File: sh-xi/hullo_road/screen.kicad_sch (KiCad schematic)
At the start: 512 parts

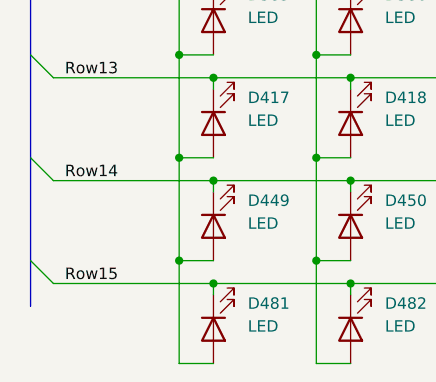
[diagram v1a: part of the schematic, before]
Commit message: Place LEDs in a grid
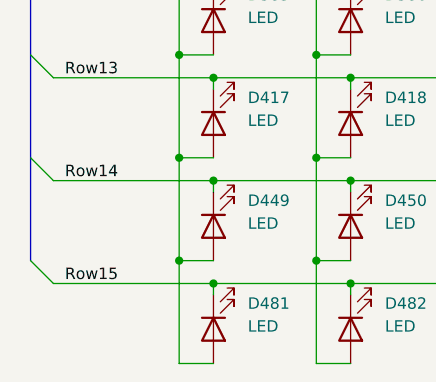
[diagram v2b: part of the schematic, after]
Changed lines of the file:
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@@
-		)
-	)
-	(bus
-		(pts
-			(xy 38.1 222.25) (xy 38.1 227.33)
-		)
-		(stroke
-			(width 0)
-			(type default)
 		)
 	)

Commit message: Create two board design and route most things
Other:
- added sheet Screen Connectors (screen_connectors.kicad_sch)
